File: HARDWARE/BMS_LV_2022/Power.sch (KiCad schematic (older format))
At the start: 19 parts, among them U2 LM1117-3.3, U3 LMR23610

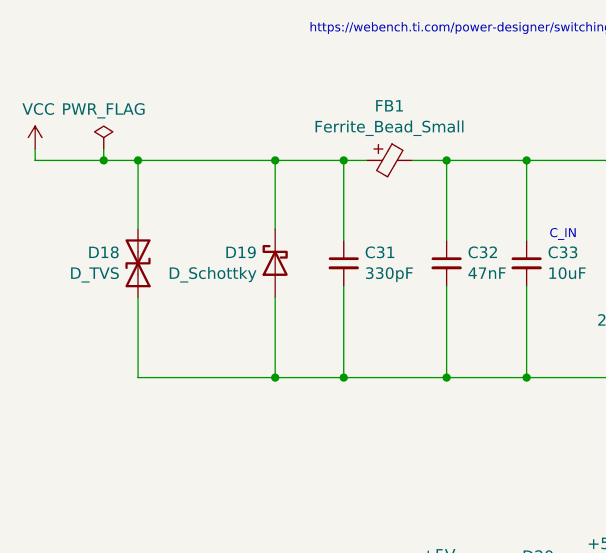
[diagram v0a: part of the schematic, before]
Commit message: Thermistors change
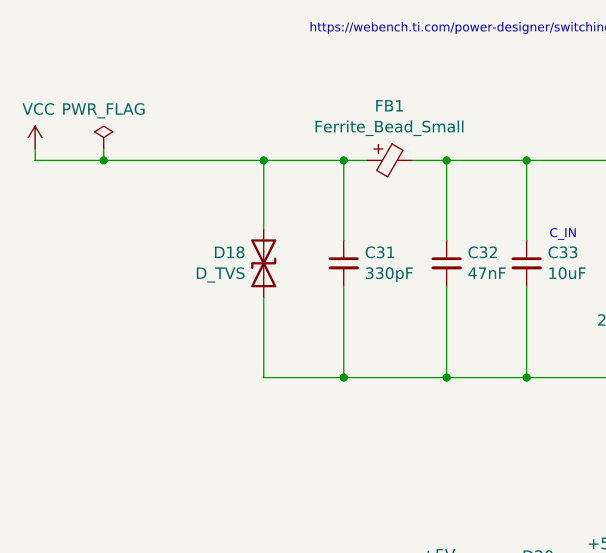
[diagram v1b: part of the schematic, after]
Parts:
- removed D19: D_Schottky, Diode_SMD:D_SMB, symbol Device:D_Schottky
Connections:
- wire segments 84 -> 80
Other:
- moved on the sheet: D18
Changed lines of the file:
@@
 	6150 4200 6300 4200
 Connection ~ 6300 4200
-$Comp
-L Device:D_Schottky D19
-U 1 1 627C310B
-P 4000 3800
-F 0 "D19" V 3954 3880 50  0000 L CNN
-F 1 "D_Schottky" V 4045 3880 50  0000 L CNN
-F 2 "Diode_SMD:D_SMB" H 4000 3800 50  0001 C CNN
-F 3 "~" H 4000 3800 50  0001 C CNN
-	1    4000 3800
-	0    -1   1    0
-$EndComp
 Connection ~ 5100 3350
 Wire Wire Line
@@
 L Device:D_TVS D18
 U 1 1 61BBDDDA
-P 3400 3800
-F 0 "D18" V 3446 3720 50  0000 R CNN
-F 1 "D_TVS" V 3355 3720 50  0000 R CNN
-F 2 "Diode_SMD:D_SMB" H 3400 3800 50  0001 C CNN
-F 3 "~" H 3400 3800 50  0001 C CNN
-	1    3400 3800
+P 3950 3800
+F 0 "D18" V 3996 3720 50  0000 R CNN
+F 1 "D_TVS" V 3905 3720 50  0000 R CNN
+F 2 "Diode_SMD:D_SMB" H 3950 3800 50  0001 C CNN
+F 3 "~" H 3950 3800 50  0001 C CNN
+	1    3950 3800
 	0    1    -1   0
 $EndComp
@@
 	2950 3350 3250 3350
 Wire Wire Line
-	3400 3350 3400 3650
-Wire Wire Line
-	3400 4300 4000 4300
-Wire Wire Line
-	3400 3950 3400 4300
-Connection ~ 3400 3350
-Wire Wire Line
-	3400 3350 4000 3350
-Wire Wire Line
-	4000 4300 4000 3950
-Wire Wire Line
-	4000 3650 4000 3350
-Connection ~ 4000 4300
-Wire Wire Line
-	4000 4300 4300 4300
-Connection ~ 4000 3350
-Wire Wire Line
-	4000 3350 4300 3350
+	3950 3350 3950 3650
+Wire Wire Line
+	3950 3950 3950 4300
 $Comp
 L Device:C_Small C40
@@
 	3250 3300 3250 3350
 Connection ~ 3250 3350
-Wire Wire Line
-	3250 3350 3400 3350
 $Comp
 L power:PWR_FLAG #FLG0105
@@
 Wire Wire Line
 	6600 5300 6950 5300
+Connection ~ 3950 3350
+Wire Wire Line
+	3950 3350 4300 3350
+Wire Wire Line
+	3950 4300 4300 4300
+Wire Wire Line
+	3250 3350 3950 3350
 $EndSCHEMATC

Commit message: PCB update
Parts changed due to smaller footprints
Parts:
- removed U2: LM1117-3.3, Package_TO_SOT_SMD:SOT-223-3_TabPin2, symbol Regulator_Linear:LM1117-3.3
- added C44: 100nF, Capacitor_SMD:C_0603_1608Metric, symbol Device:C_Small
- added U2: LD3985M33R_TSOT23, Package_TO_SOT_SMD:TSOT-23-5, symbol Regulator_Linear:LD3985G18R_TSOT23
- C34, C36: value 100nF -> 1uF
- C38: footprint Capacitor_SMD:CP_Elec_6.3x7.7 -> Capacitor_Tantalum_SMD:CP_EIA-6032-28_Kemet-C; Part Number (none) -> TPSC107K010R0100
- D20: footprint Diode_SMD:D_SMB -> Diode_SMD:D_SOD-123; Part Number (none) -> SD103BW
- L2: footprint Inductor_SMD:L_12x12mm_H8mm -> Inductor_SMD:L_7.3x7.3_H4.5; Part Number (none) -> 7447779122
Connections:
- wire segments 80 -> 87
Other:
- moved on the sheet: C34, C36
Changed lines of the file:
@@
-$EndComp
-$Comp
-L Regulator_Linear:LM1117-3.3 U2
-U 1 1 61DB7955
-P 6150 5300
-F 0 "U2" H 6150 5542 50  0000 C CNN
-F 1 "LM1117-3.3" H 6150 5451 50  0000 C CNN
-F 2 "Package_TO_SOT_SMD:SOT-223-3_TabPin2" H 6150 5300 50  0001 C CNN
-F 3 "http://www.ti.com/lit/ds/symlink/lm1117.pdf" H 6150 5300 50  0001 C CNN
-	1    6150 5300
-	1    0    0    -1
 $EndComp
 $Comp
 L Device:C_Small C36
 U 1 1 61DBD742
-P 6600 5450
-F 0 "C36" H 6692 5496 50  0000 L CNN
-F 1 "100nF" H 6692 5405 50  0000 L CNN
-F 2 "Capacitor_SMD:C_0603_1608Metric" H 6600 5450 50  0001 C CNN
-F 3 "~" H 6600 5450 50  0001 C CNN
-	1    6600 5450
+P 7100 5600
+F 0 "C36" H 7192 5646 50  0000 L CNN
+F 1 "1uF" H 7192 5555 50  0000 L CNN
+F 2 "Capacitor_SMD:C_0603_1608Metric" H 7100 5600 50  0001 C CNN
+F 3 "~" H 7100 5600 50  0001 C CNN
+	1    7100 5600
 	1    0    0    -1
 $EndComp
@@
 L Device:C_Small C34
 U 1 1 61DBF04E
-P 5700 5450
-F 0 "C34" H 5608 5404 50  0000 R CNN
-F 1 "100nF" H 5608 5495 50  0000 R CNN
-F 2 "Capacitor_SMD:C_0603_1608Metric" H 5700 5450 50  0001 C CNN
-F 3 "~" H 5700 5450 50  0001 C CNN
-	1    5700 5450
+P 5600 5600
+F 0 "C34" H 5508 5554 50  0000 R CNN
+F 1 "1uF" H 5508 5645 50  0000 R CNN
+F 2 "Capacitor_SMD:C_0603_1608Metric" H 5600 5600 50  0001 C CNN
+F 3 "~" H 5600 5600 50  0001 C CNN
+	1    5600 5600
 	1    0    0    1
 $EndComp
 Wire Wire Line
-	5850 5300 5700 5300
-Wire Wire Line
-	5700 5300 5700 5350
-Wire Wire Line
-	5700 5550 5700 5650
-Wire Wire Line
-	5700 5650 6150 5650
-Wire Wire Line
-	6600 5650 6600 5550
-Wire Wire Line
-	6150 5600 6150 5650
-Connection ~ 6150 5650
-Wire Wire Line
-	6150 5650 6600 5650
-Wire Wire Line
-	6150 5650 6150 5700
-Connection ~ 5700 5300
+	5850 5300 5800 5300
 Wire Wire Line
 	4700 5300 4700 5250
-Wire Wire Line
-	6600 5350 6600 5300
-Wire Wire Line
-	6600 5300 6450 5300
 $Comp
 L power:+5V #PWR041
@@
 	1    0    0    -1
 $EndComp
-$Comp
-L power:GND #PWR043
-U 1 1 61DCFD15
-P 6150 5700
-F 0 "#PWR043" H 6150 5450 50  0001 C CNN
-F 1 "GND" H 6155 5527 50  0000 C CNN
-F 2 "" H 6150 5700 50  0001 C CNN
-F 3 "" H 6150 5700 50  0001 C CNN
-	1    6150 5700
-	1    0    0    -1
-$EndComp
 Wire Wire Line
 	5450 5300 5450 5200
 Connection ~ 5450 5300
 Wire Wire Line
-	5450 5300 5700 5300
+	5450 5300 5600 5300
 $Comp
 L power:+5VD #PWR042
@@
 F 0 "L2" V 7585 3650 50  0000 C CNN
 F 1 "22u" V 7494 3650 50  0000 C CNN
-F 2 "Inductor_SMD:L_12x12mm_H8mm" H 7400 3650 50  0001 C CNN
+F 2 "Inductor_SMD:L_7.3x7.3_H4.5" H 7400 3650 50  0001 C CNN
 F 3 "~" H 7400 3650 50  0001 C CNN
+F 4 "7447779122" H 7400 3650 50  0001 C CNN "Part Number"
 	1    7400 3650
 	0    -1   -1   0
@@
 F 0 "C38" H 8188 3996 50  0000 L CNN
 F 1 "100uF" H 8188 3905 50  0000 L CNN
-F 2 "Capacitor_SMD:CP_Elec_6.3x7.7" H 8100 3950 50  0001 C CNN
+F 2 "Capacitor_Tantalum_SMD:CP_EIA-6032-28_Kemet-C" H 8100 3950 50  0001 C CNN
 F 3 "~" H 8100 3950 50  0001 C CNN
+F 4 "TPSC107K010R0100" H 8100 3950 50  0001 C CNN "Part Number"
 	1    8100 3950
 	1    0    0    -1
@@
 L power:+3.3V #PWR045
 U 1 1 61DCDF1D
-P 6950 5250
-F 0 "#PWR045" H 6950 5100 50  0001 C CNN
-F 1 "+3.3V" H 6965 5423 50  0000 C CNN
-F 2 "" H 6950 5250 50  0001 C CNN
-F 3 "" H 6950 5250 50  0001 C CNN
-	1    6950 5250
-	1    0    0    -1
-$EndComp
-Wire Wire Line
-	6950 5300 6950 5250
+P 7250 5250
+F 0 "#PWR045" H 7250 5100 50  0001 C CNN
+F 1 "+3.3V" H 7265 5423 50  0000 C CNN
+F 2 "" H 7250 5250 50  0001 C CNN
+F 3 "" H 7250 5250 50  0001 C CNN
+	1    7250 5250
+	1    0    0    -1
+$EndComp
+Wire Wire Line
+	7250 5300 7250 5250
 Wire Wire Line
 	4700 5300 5000 5300
@@
 F 0 "D20" H 5150 5083 50  0000 C CNN
 F 1 "D_Schottky" H 5150 5174 50  0000 C CNN
-F 2 "Diode_SMD:D_SMB" H 5150 5300 50  0001 C CNN
+F 2 "Diode_SMD:D_SOD-123" H 5150 5300 50  0001 C CNN
 F 3 "~" H 5150 5300 50  0001 C CNN
+F 4 "SD103BW" H 5150 5300 50  0001 C CNN "Part Number"
 	1    5150 5300
 	-1   0    0    1
 $EndComp
-Connection ~ 6600 5300
-Wire Wire Line
-	6600 5300 6950 5300
 Connection ~ 3950 3350
 Wire Wire Line
@@
 Wire Wire Line
 	3250 3350 3950 3350
+$Comp
+L Regulator_Linear:LD3985G18R_TSOT23 U2
+U 1 1 61D3894B
+P 6150 5400
+F 0 "U2" H 6150 5742 50  0000 C CNN
+F 1 "LD3985M33R_TSOT23" H 6150 5651 50  0000 C CNN
+F 2 "Package_TO_SOT_SMD:TSOT-23-5" H 6150 5725 50  0001 C CIN
+F 3 "https://pdf1.alldatasheet.com/datasheet-pdf/view/85510/STMICROELECTRONICS/LD3985M33R.html" H 6150 5450 50  0001 C CNN
+F 4 "LDS3985M33R" H 6150 5651 50  0001 C CNN "Part Number"
+	1    6150 5400
+	1    0    0    -1
+$EndComp
+$Comp
+L power:GND #PWR043
+U 1 1 61DCFD15
+P 6150 5900
+F 0 "#PWR043" H 6150 5650 50  0001 C CNN
+F 1 "GND" H 6155 5727 50  0000 C CNN
+F 2 "" H 6150 5900 50  0001 C CNN
+F 3 "" H 6150 5900 50  0001 C CNN
+	1    6150 5900
+	1    0    0    -1
+$EndComp
+Wire Wire Line
+	6150 5850 6150 5900
+Connection ~ 6150 5850
+Wire Wire Line
+	5850 5400 5800 5400
+Wire Wire Line
+	5800 5400 5800 5300
+Connection ~ 5800 5300
+$Comp
+L Device:C_Small C44
+U 1 1 61D502E1
+P 6650 5600
+F 0 "C44" H 6742 5646 50  0000 L CNN
+F 1 "100nF" H 6742 5555 50  0000 L CNN
+F 2 "Capacitor_SMD:C_0603_1608Metric" H 6650 5600 50  0001 C CNN
+F 3 "~" H 6650 5600 50  0001 C CNN
+	1    6650 5600
+	1    0    0    -1
+$EndComp
+Wire Wire Line
+	6450 5400 6650 5400
+Wire Wire Line
+	6650 5400 6650 5500
+Wire Wire Line
+	6650 5700 6650 5850
+Wire Wire Line
+	6150 5850 6650 5850
+Connection ~ 6650 5850
+Wire Wire Line
+	7100 5850 7100 5700
+Wire Wire Line
+	6650 5850 7100 5850
+Wire Wire Line
+	7100 5300 7100 5500
+Wire Wire Line
+	6450 5300 7100 5300
+Wire Wire Line
+	7100 5300 7250 5300
+Connection ~ 7100 5300
+Wire Wire Line
+	6150 5700 6150 5850
+Connection ~ 5600 5300
+Wire Wire Line
+	5600 5300 5800 5300
+Wire Wire Line
+	5600 5850 6150 5850
+Wire Wire Line
+	5600 5300 5600 5500
+Wire Wire Line
+	5600 5700 5600 5850
 $EndSCHEMATC

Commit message: PCB Routing Update 2
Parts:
- U3: symbol BMS_LV_2022-rescue:LMR23610-LMR23610 -> LMR23610:LMR23610
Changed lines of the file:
@@
 $EndComp
 $Comp
-L BMS_LV_2022-rescue:LMR23610-LMR23610 U?
+L LMR23610:LMR23610 U?
 U 1 1 626F8D84
 P 6250 3550
